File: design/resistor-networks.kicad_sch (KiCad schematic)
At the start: 124 parts

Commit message: Footprint assignment / part selection
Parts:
- renumbered RP_A82 to RP_A10, RP_A3 to RP_A11, RP_A23 to RP_A12, RP_A43 to RP_A13, RP_A63 to RP_A14, RP_A83 to RP_A15, RP_A4 to RP_A16, RP_A24 to RP_A17, RP_A44 to RP_A18, RP_A64 to RP_A19, RP_A21 to RP_A2, RP_A84 to RP_A20, RP_A5 to RP_A21, RP_A25 to RP_A22, RP_A45 to RP_A23, RP_A65 to RP_A24, RP_A85 to RP_A25, RP_A6 to RP_A26, RP_A26 to RP_A27, RP_A46 to RP_A28, RP_A66 to RP_A29, RP_A41 to RP_A3, RP_A86 to RP_A30, RP_A7 to RP_A31, RP_A27 to RP_A32, RP_A47 to RP_A33, RP_A67 to RP_A34, RP_A87 to RP_A35, RP_A8 to RP_A36, RP_A28 to RP_A37, RP_A48 to RP_A38, RP_A68 to RP_A39, RP_A61 to RP_A4, RP_A88 to RP_A40, RP_A9 to RP_A41, RP_A29 to RP_A42, RP_A49 to RP_A43, RP_A69 to RP_A44, RP_A89 to RP_A45, RP_A10 to RP_A46, RP_A30 to RP_A47, RP_A50 to RP_A48, RP_A70 to RP_A49, RP_A81 to RP_A5, RP_A90 to RP_A50, RP_A11 to RP_A51, RP_A31 to RP_A52, RP_A51 to RP_A53, RP_A71 to RP_A54, RP_A91 to RP_A55, RP_A12 to RP_A56, RP_A32 to RP_A57, RP_A52 to RP_A58, RP_A72 to RP_A59, RP_A2 to RP_A6, RP_A92 to RP_A60, RP_A13 to RP_A61, RP_A33 to RP_A62, RP_A53 to RP_A63, RP_A73 to RP_A64, RP_A93 to RP_A65, RP_A14 to RP_A66, RP_A34 to RP_A67, RP_A54 to RP_A68, RP_A74 to RP_A69, RP_A22 to RP_A7, RP_A94 to RP_A70, RP_A15 to RP_A71, RP_A35 to RP_A72, RP_A55 to RP_A73, RP_A75 to RP_A74, RP_A95 to RP_A75, RP_A16 to RP_A76, RP_A36 to RP_A77, RP_A56 to RP_A78, RP_A76 to RP_A79, RP_A42 to RP_A8, RP_A96 to RP_A80, RP_A17 to RP_A81, RP_A37 to RP_A82, RP_A57 to RP_A83, RP_A77 to RP_A84, RP_A97 to RP_A85, RP_A18 to RP_A86, RP_A38 to RP_A87, RP_A58 to RP_A88, RP_A78 to RP_A89, RP_A62 to RP_A9, RP_A98 to RP_A90, RP_A19 to RP_A91, RP_A39 to RP_A92, RP_A59 to RP_A93, RP_A79 to RP_A94, RP_A99 to RP_A95, RP_A20 to RP_A96, RP_A40 to RP_A97, RP_A60 to RP_A98, RP_A80 to RP_A99, RP_B9 to RP_B10, RP_B15 to RP_B11, RP_B21 to RP_B12, RP_B4 to RP_B13, RP_B10 to RP_B14, RP_B16 to RP_B15, RP_B22 to RP_B16, RP_B5 to RP_B17, RP_B11 to RP_B18, RP_B17 to RP_B19, RP_B7 to RP_B2, RP_B23 to RP_B20, RP_B6 to RP_B21, RP_B12 to RP_B22, RP_B18 to RP_B23, RP_B13 to RP_B3, RP_B19 to RP_B4, RP_B2 to RP_B5, RP_B8 to RP_B6, RP_B14 to RP_B7, RP_B20 to RP_B8, RP_B3 to RP_B9

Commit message: More footprint assignment and component selection
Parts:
- RP_A1, RP_A10, RP_A100, RP_A11, RP_A12, RP_A13, RP_A14, RP_A15, RP_A16, RP_A17, RP_A18, RP_A19, RP_A2, RP_A20, RP_A21, RP_A22, RP_A23, RP_A24, RP_A25, RP_A26, RP_A27, RP_A28, RP_A29, RP_A3, RP_A30, RP_A31, RP_A32, RP_A33, RP_A34, RP_A35, RP_A36, RP_A37, RP_A38, RP_A39, RP_A4, RP_A40, RP_A41, RP_A42, RP_A43, RP_A44, RP_A45, RP_A46, RP_A47, RP_A48, RP_A49, RP_A5, RP_A50, RP_A51, RP_A52, RP_A53, RP_A54, RP_A55, RP_A56, RP_A57, RP_A58, RP_A59, RP_A6, RP_A60, RP_A61, RP_A62, RP_A63, RP_A64, RP_A65, RP_A66, RP_A67, RP_A68, RP_A69, RP_A7, RP_A70, RP_A71, RP_A72, RP_A73, RP_A74, RP_A75, RP_A76, RP_A77, RP_A78, RP_A79, RP_A8, RP_A80, RP_A81, RP_A82, RP_A83, RP_A84, RP_A85, RP_A86, RP_A87, RP_A88, RP_A89, RP_A9, RP_A90, RP_A91, RP_A92, RP_A93, RP_A94, RP_A95, RP_A96, RP_A97, RP_A98, RP_A99, RP_B1, RP_B10, RP_B11, RP_B12, RP_B13, RP_B14, RP_B15, RP_B16, RP_B17, RP_B18, RP_B19, RP_B2, RP_B20, RP_B21, RP_B22, RP_B23, RP_B24, RP_B3, RP_B4, RP_B5, RP_B6, RP_B7, RP_B8, RP_B9: footprint (none) -> Resistor_SMD:R_2512_6332Metric

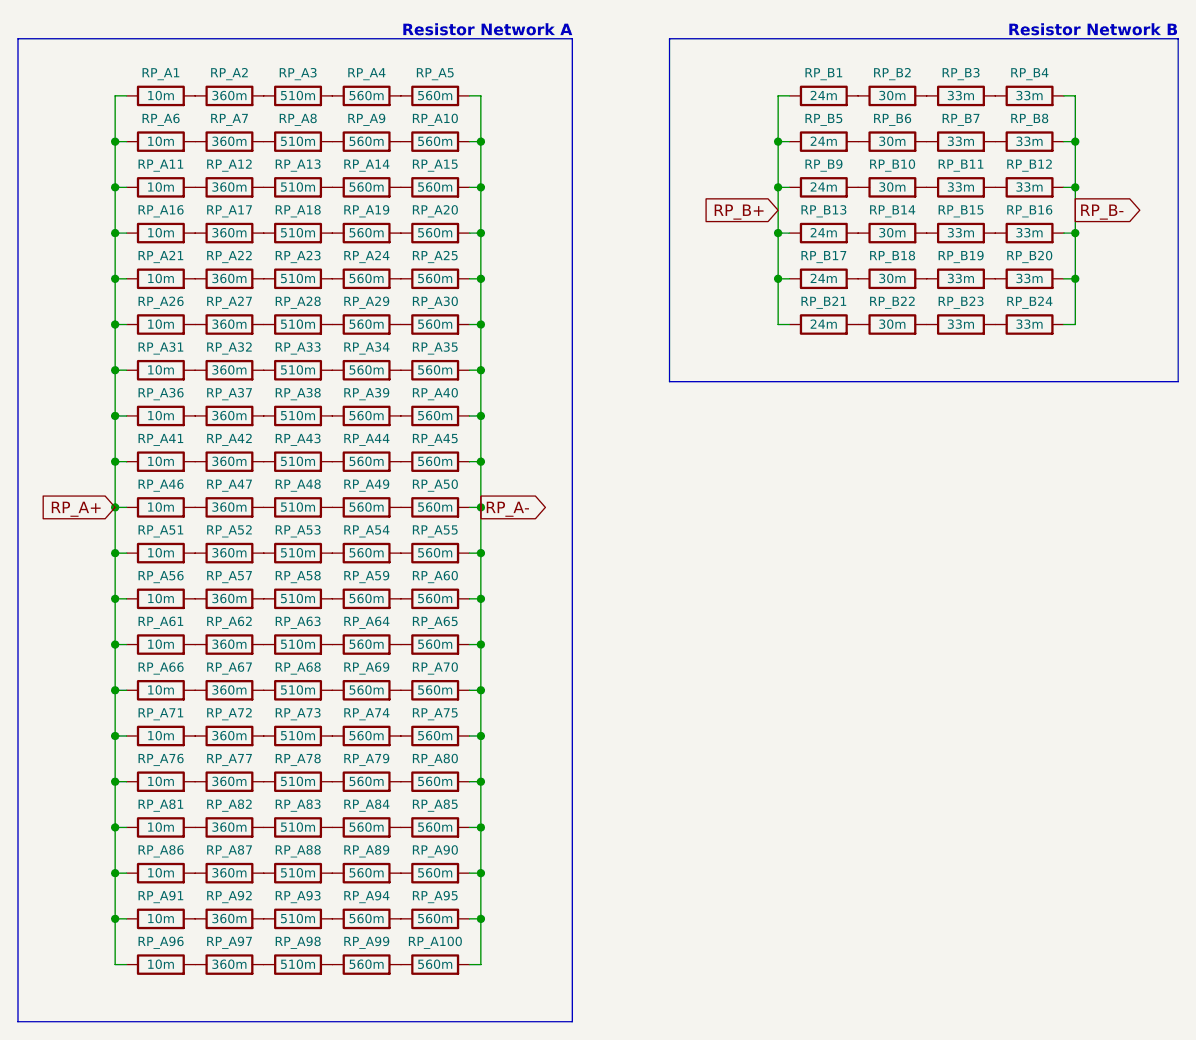
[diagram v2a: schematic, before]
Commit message: Swapped resistor networks for shunt resistors
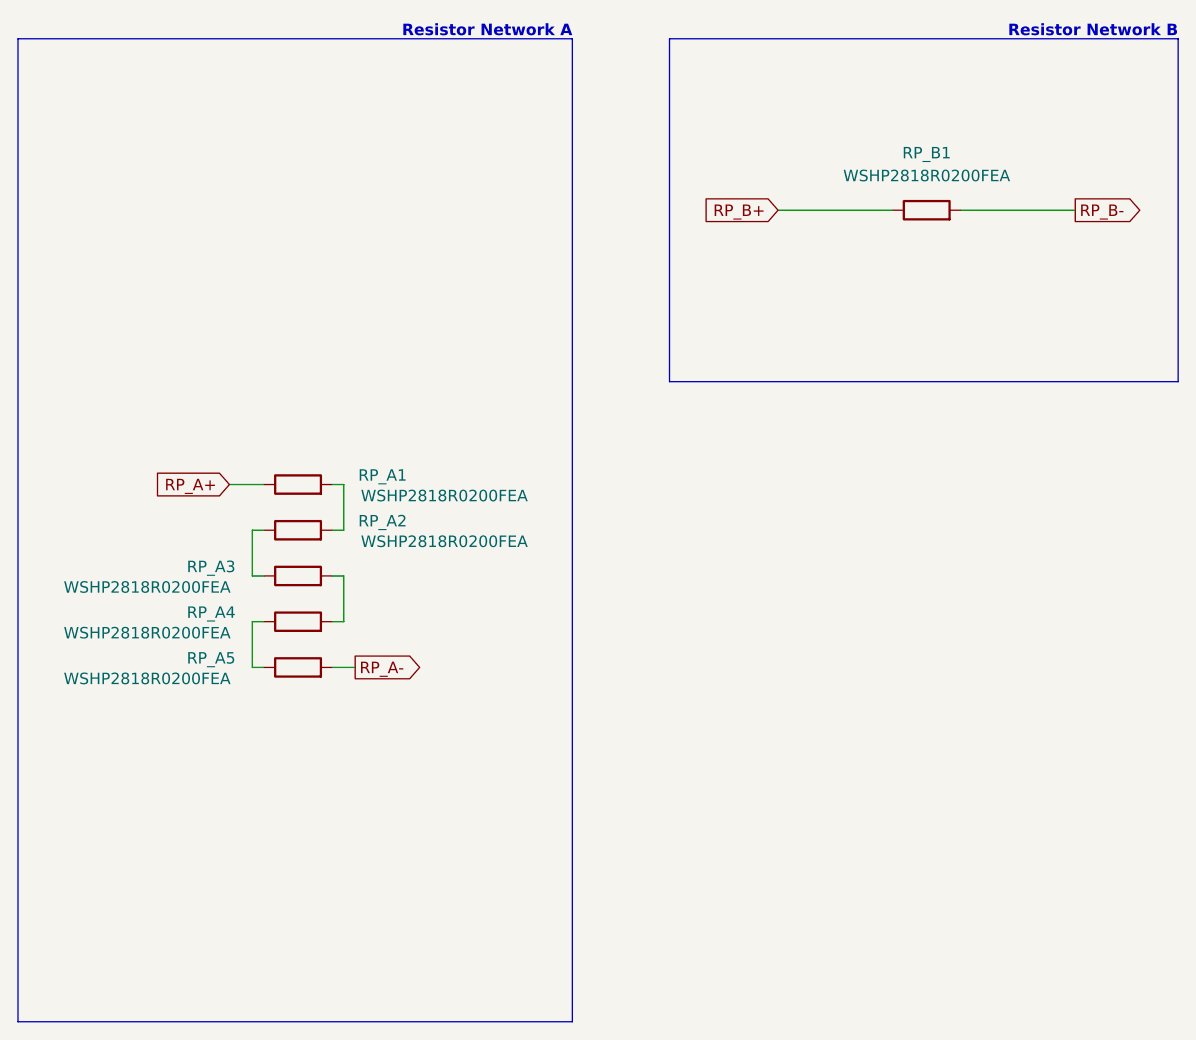
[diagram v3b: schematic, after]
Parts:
- removed RP_A10, RP_A100, RP_A14, RP_A15, RP_A19, RP_A20, RP_A24, RP_A25, RP_A29, RP_A30, RP_A34, RP_A35, RP_A39, RP_A40, RP_A44, RP_A45, RP_A49, RP_A50, RP_A54, RP_A55, RP_A59, RP_A60, RP_A64, RP_A65, RP_A69, RP_A70, RP_A74, RP_A75, RP_A79, RP_A80, RP_A84, RP_A85, RP_A89, RP_A9, RP_A90, RP_A94, RP_A95, RP_A99: 560m, Resistor_SMD:R_2512_6332Metric, symbol Device:R
- removed RP_A11, RP_A16, RP_A21, RP_A26, RP_A31, RP_A36, RP_A41, RP_A46, RP_A51, RP_A56, RP_A6, RP_A61, RP_A66, RP_A71, RP_A76, RP_A81, RP_A86, RP_A91, RP_A96: 10m, Resistor_SMD:R_2512_6332Metric, symbol Device:R
- removed RP_A12, RP_A17, RP_A22, RP_A27, RP_A32, RP_A37, RP_A42, RP_A47, RP_A52, RP_A57, RP_A62, RP_A67, RP_A7, RP_A72, RP_A77, RP_A82, RP_A87, RP_A92, RP_A97: 360m, Resistor_SMD:R_2512_6332Metric, symbol Device:R
- removed RP_A13, RP_A18, RP_A23, RP_A28, RP_A33, RP_A38, RP_A43, RP_A48, RP_A53, RP_A58, RP_A63, RP_A68, RP_A73, RP_A78, RP_A8, RP_A83, RP_A88, RP_A93, RP_A98: 510m, Resistor_SMD:R_2512_6332Metric, symbol Device:R
- removed RP_B10, RP_B14, RP_B18, RP_B2, RP_B22, RP_B6: 30m, Resistor_SMD:R_2512_6332Metric, symbol Device:R
- removed RP_B11, RP_B12, RP_B15, RP_B16, RP_B19, RP_B20, RP_B23, RP_B24, RP_B3, RP_B4, RP_B7, RP_B8: 33m, Resistor_SMD:R_2512_6332Metric, symbol Device:R
- removed RP_B13, RP_B17, RP_B21, RP_B5, RP_B9: 24m, Resistor_SMD:R_2512_6332Metric, symbol Device:R
- RP_A1: value 10m -> WSHP2818R0200FEA; footprint Resistor_SMD:R_2512_6332Metric -> project-footprints:WSHP2818R0200FEA
- RP_A2: value 360m -> WSHP2818R0200FEA; footprint Resistor_SMD:R_2512_6332Metric -> project-footprints:WSHP2818R0200FEA
- RP_A3: value 510m -> WSHP2818R0200FEA; footprint Resistor_SMD:R_2512_6332Metric -> project-footprints:WSHP2818R0200FEA
- RP_A4, RP_A5: value 560m -> WSHP2818R0200FEA; footprint Resistor_SMD:R_2512_6332Metric -> project-footprints:WSHP2818R0200FEA
- RP_B1: value 24m -> WSHP2818R0200FEA; footprint Resistor_SMD:R_2512_6332Metric -> project-footprints:WSHP2818R0200FEA
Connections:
- net RP_B-: now also RP_B1.2
- net at RP_A2.2: now also RP_A1.2; no longer RP_A3.1
- net at RP_A4.1: now also RP_A5.1; no longer RP_A3.2
- net at RP_A4.2: now also RP_A3.2; no longer RP_A5.1
- net at RP_A2.1: now also RP_A3.1; no longer RP_A1.2

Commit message: _
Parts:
- removed RP_A2, RP_A3, RP_A4, RP_A5: WSHP2818R0200FEA, project-footprints:WSHP2818R0200FEA, symbol Device:R
- RP_A1: value WSHP2818R0200FEA -> PF2472-0R1F1; footprint project-footprints:WSHP2818R0200FEA -> Package_TO_SOT_THT:TO-247-2_Horizontal_TabDown
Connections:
- net RP_A-: now also RP_A1.2

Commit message: Fixing layout and parts selection issues for prototype run
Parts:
- removed RP_A1: PF2472-0R1F1, Package_TO_SOT_THT:TO-247-2_Horizontal_TabDown, symbol Device:R
- removed RP_B1: WSHP2818R0200FEA, project-footprints:WSHP2818R0200FEA, symbol Device:R
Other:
- note removed: "Resistor Network A"
- note removed: "Resistor Network B"
